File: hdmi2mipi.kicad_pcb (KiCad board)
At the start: 4 copper layers, 45.2 x 47.2 mm, 97 parts, among them J1 IO, J2 HDMI_A_1.4, J8 AudioJack3, J9 QWIIC, Q1 BC846, Q2 BC846, Q3 BC846, Q4 BC846, Q5 BC846, Q6 BC846, Q7 2SC2712, U10 SY8079AAC, U11 SY8079AAC, U8 MS4344, U9 SY8079AAC, X1 SG-210STF

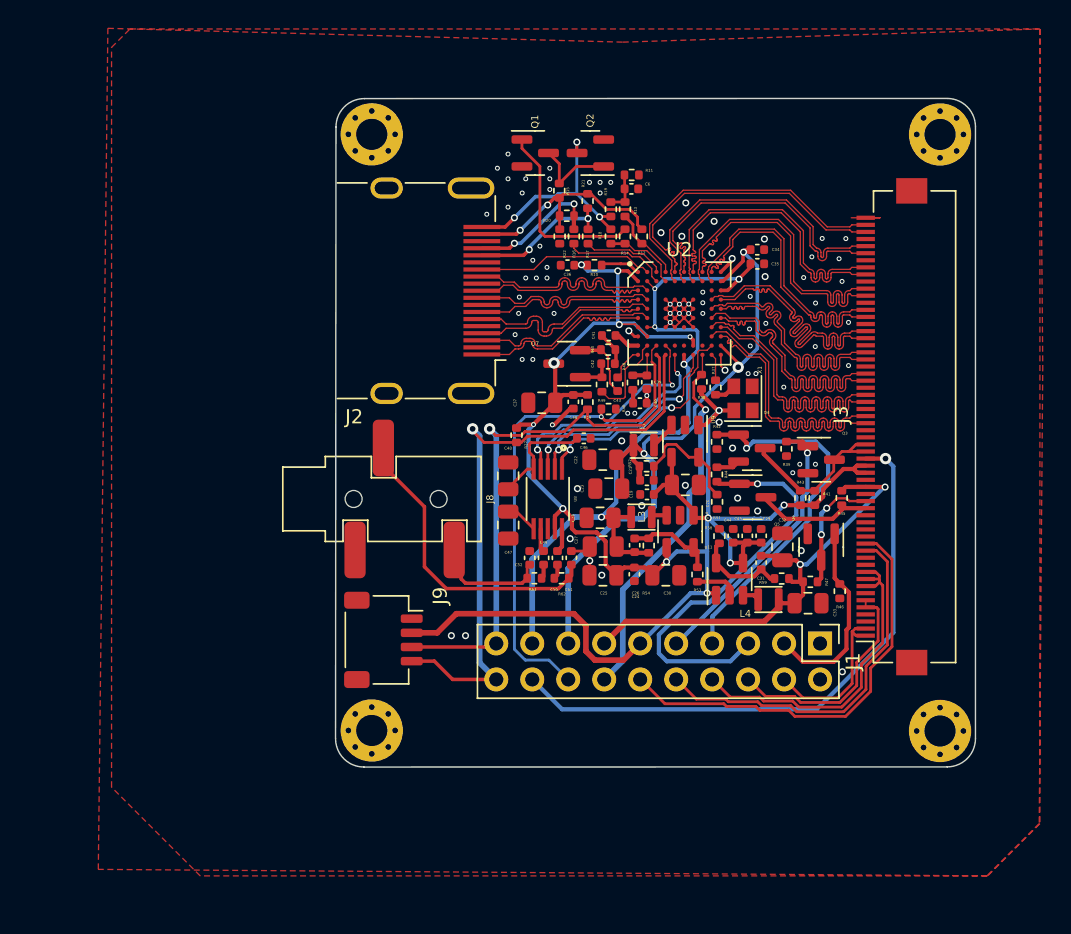
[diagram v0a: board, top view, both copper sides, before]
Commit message: Changed copper layers, heaps of other issues.
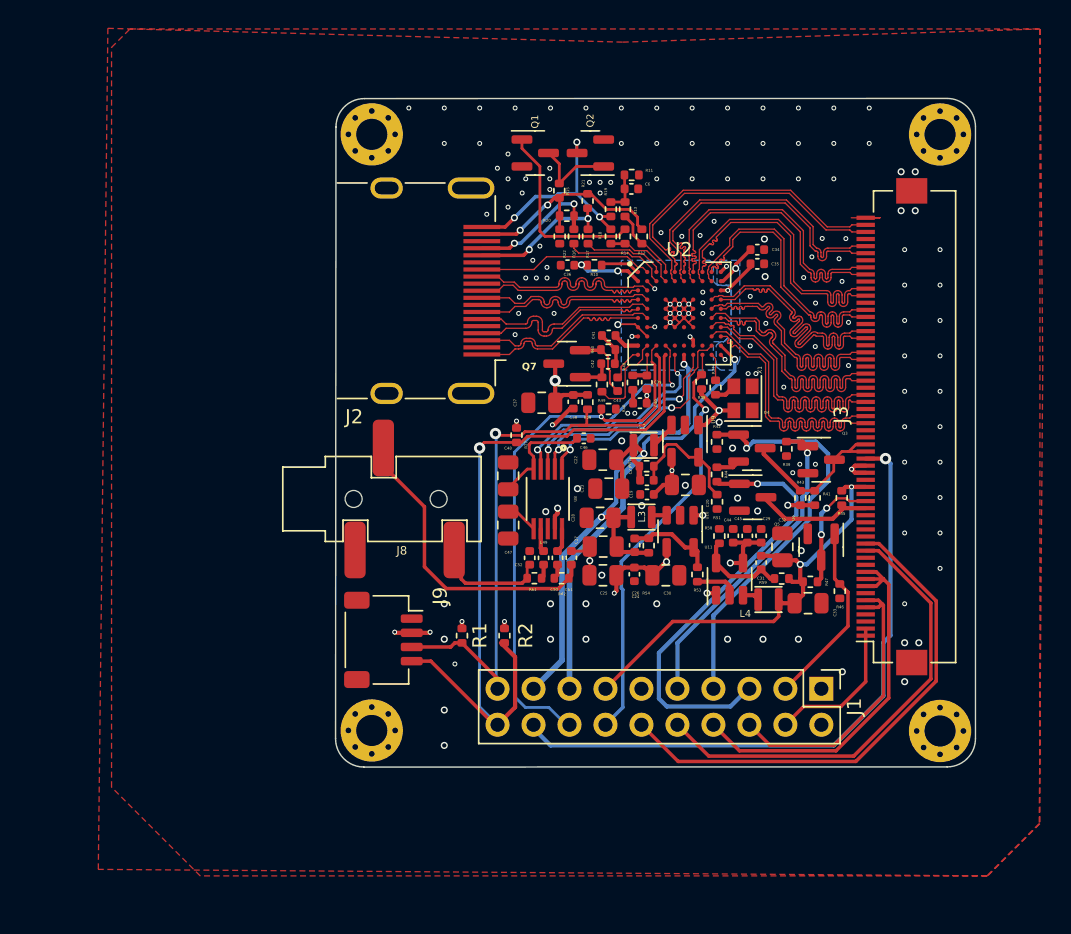
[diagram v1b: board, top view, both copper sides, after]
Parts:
- added R1: 2k, Resistor_SMD:R_0402_1005Metric, F.Cu at (-8.75, 12.2)
- added R2: 2k, Resistor_SMD:R_0402_1005Metric, F.Cu at (-5.75, 12.2)
- moved J1 3.20 mm to (16.6, 16.0)
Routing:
- net 3V3_HDMI: track 130.3 -> 44.8 mm, vias 13 -> 20
- net +1V1: track 54.3 -> 41.5 mm
- net SCL: track 44.1 -> 52.6 mm
- net +1V2: track 49.3 -> 41.4 mm
- net Net-(J1-Pin_12): track 30.3 -> 36.5 mm
- net Net-(J1-Pin_10): track 26.5 -> 32.6 mm
- net SDA: track 39.3 -> 43.9 mm
- net Net-(J1-Pin_6): track 16.3 -> 20.6 mm
- net 3V3_S2: track 18.8 -> 22.6 mm
- net Net-(J1-Pin_8): track 23.6 -> 27.4 mm
- net RESET: track 26.4 -> 29.6 mm
- net 3V3_S1: track 25.8 -> 29.0 mm
- net VIN: track 42.5 -> 45.1 mm
- net 1V8_S2: track 28.9 -> 31.4 mm
- net GND: track 33.2 -> 30.8 mm, vias 86 -> 152
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- added copper zone on B.Cu, net +1V1
- added copper zone on B.Cu, net +1V2
- removed copper zone on In2.Cu, net +1V1
- removed copper zone on In2.Cu, net +1V2

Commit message: Fixed many warnings and errors.
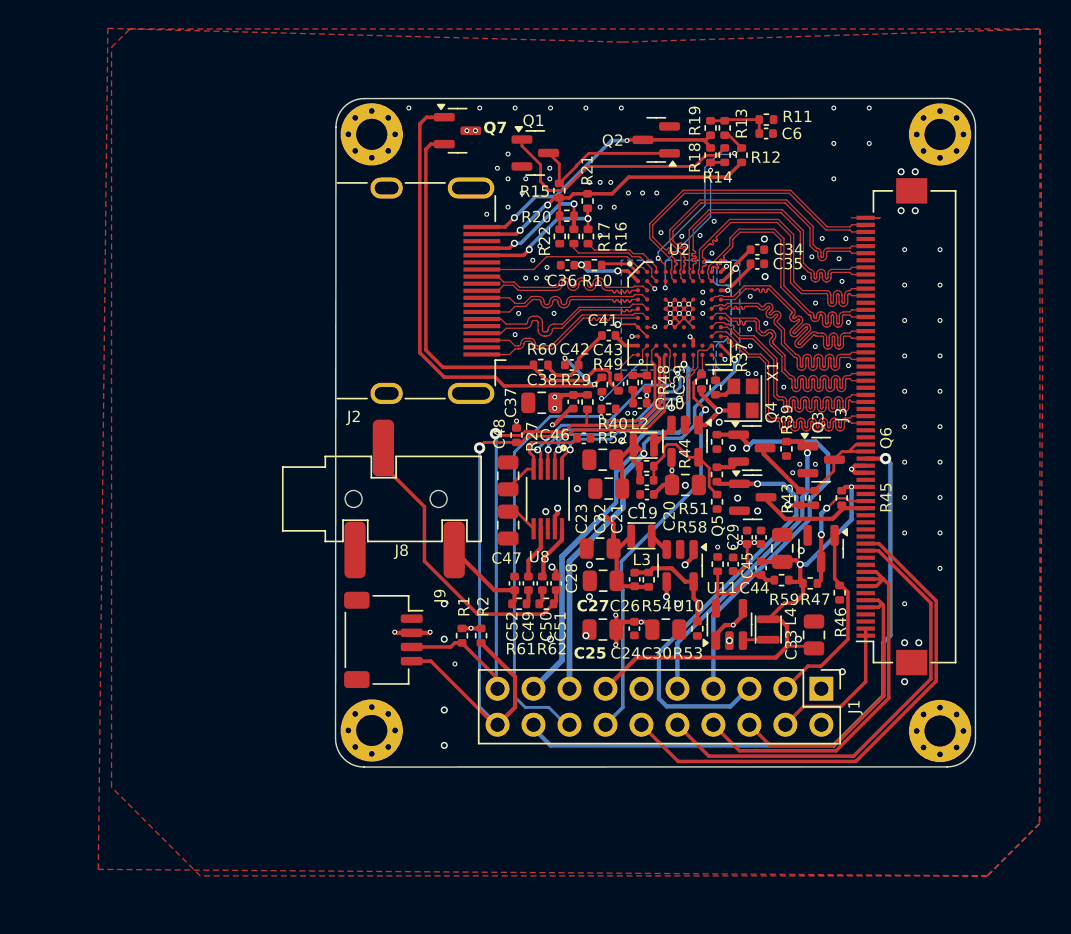
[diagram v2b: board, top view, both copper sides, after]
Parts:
- moved Q7 18.2 mm to (-9.06, -23.4), turned to 0 degrees
- moved C6 10.3 mm to (12.7, -23.2)
- moved R11 10.3 mm to (12.7, -24.2)
- moved R14 9.08 mm to (9.80, -21.7)
- moved R18 9.08 mm to (8.80, -21.7)
- moved R12 9.08 mm to (11.0, -21.7), turned to 90 degrees
- moved R13 9.08 mm to (9.80, -23.6)
- moved R19 9.08 mm to (8.80, -23.6)
- moved R60 4.88 mm to (-3.19, -6.86)
- moved Q2 4.74 mm to (4.96, -22.8)
- moved C24 3.83 mm to (3.42, 11.8)
- moved C25 3.83 mm to (1.20, 11.8)
- moved C30 3.83 mm to (5.64, 11.8)
- moved R53 3.83 mm to (7.87, 11.8)
- moved U11 3.21 mm to (10.1, 11.5)
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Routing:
- net Net-(Q7-B): track 2.48 -> 35.5 mm, vias 0 -> 2
- net Net-(Q7-E): track 4.89 -> 31.5 mm
- net Net-(U2-HPDI): track 5.06 -> 13.7 mm, vias 0 -> 2
- net Net-(J2-+5V): track 16.1 -> 22.7 mm
- net Net-(U2-HPDO): track 5.30 -> 11.7 mm, vias 0 -> 2
- net GND: track 30.8 -> 25.6 mm, vias 152 -> 137
- net Net-(Q1-C): track 6.10 -> 11.2 mm
- net Net-(Q1-B): track 13.4 -> 18.0 mm
- net Net-(C41-Pad1): track 2.30 -> 5.55 mm
- net Net-(J2-HPD/HEAC-): track 16.4 -> 19.5 mm, vias 3 -> 2
- net +1V8: track 32.5 -> 35.4 mm
- net Net-(U8-AOUTR): track 1.71 -> 3.84 mm
- net Net-(U8-AOUTL): track 1.66 -> 3.74 mm
- net +1V1: track 41.5 -> 43.4 mm
- net Net-(C6-Pad1): track 2.88 -> 4.32 mm
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
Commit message: Last tweaks and order at JLC
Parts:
- moved H2 5.36 mm to (20.1, -21.1)
- moved J1 5.36 mm to (11.7, 18.1)
- moved Q5 5.36 mm to (6.83, 4.56)
- moved R18 5.36 mm to (3.86, -19.6)
- moved R19 5.36 mm to (3.86, -21.5)
- moved R43 5.36 mm to (10.2, 4.61)
- moved R60 5.36 mm to (-8.13, -4.78)
- moved C23 5.36 mm to (-3.33, 3.95)
- moved C25 5.36 mm to (-3.74, 13.9)
- moved C27 5.36 mm to (-3.72, 10.4)
- moved C29 5.36 mm to (7.42, 7.39)
- moved C31 5.36 mm to (7.42, 9.56)
- moved C33 5.36 mm to (11.2, 14.3)
- moved C36 5.36 mm to (-6.24, -11.8)
- moved C37 5.36 mm to (-8.06, -2.11)
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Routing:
- net /HDMI_C_P: track 13.3 -> 14.4 mm
- net /HDMI_C_N: track 13.4 -> 14.5 mm
- net GND: vias 137 -> 149
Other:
- board text added: "TC358870XBG HDMI TO MIPI DSI Revision 0.1 04-2024 Nicolai Electronics Badge.Team CERN-OHL-P"
